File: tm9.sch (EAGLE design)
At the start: 42 parts, among them J1 DF23C-10DP-0.5V(92), J2 DF23C-10DP-0.5V(92), U2 ARTEMIS_MODULESMD, Y1 32.768kHz

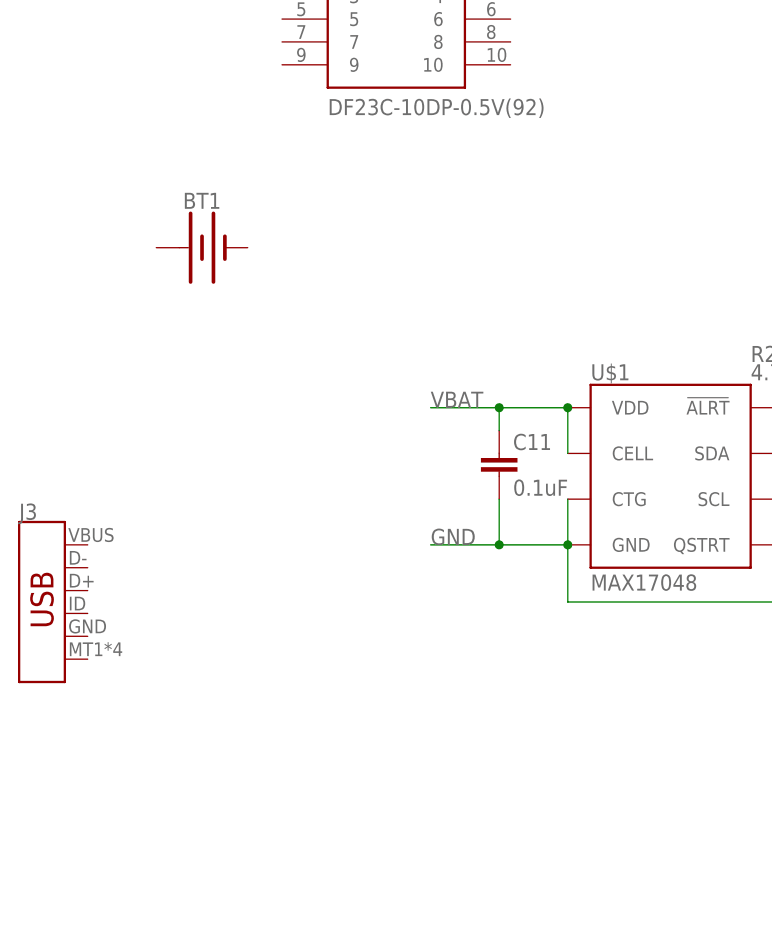
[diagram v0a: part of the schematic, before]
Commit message: rough draft
added JST-SH 6-pin RA connector, 1mA battery, and just shuffled around parts to get a general feel for things. Just a very rough draft.
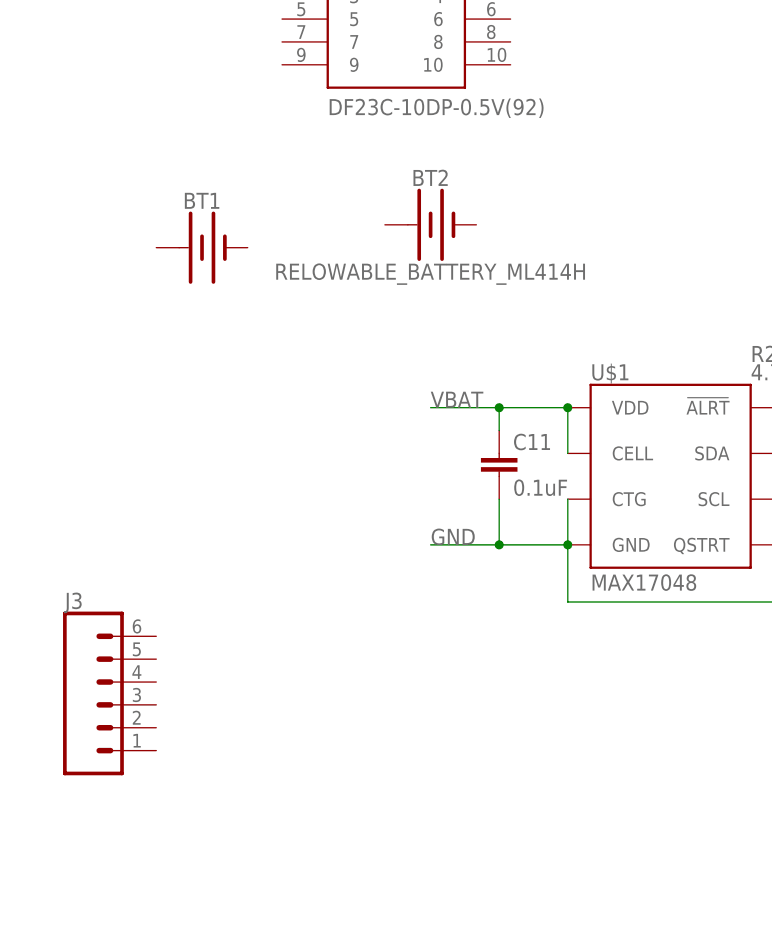
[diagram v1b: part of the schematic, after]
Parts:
- added BT2: RELOWABLE_BATTERY_ML414H, SparkFun-Batteries:RELOWABLE_BATTERY_ML414H
- J3: device SparkFun-Connectors:USB_MICRO-B_SMT -> SparkFun-Connectors:CONN_06JST-SMD-LOCKING
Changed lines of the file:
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@@
 <part name="J2" library="DF23C-10DP-0.5V_92_" deviceset="DF23C-10DP-0.5V(92)" device=""/>
 <part name="U2" library="SparkFun-IC-Microcontroller" deviceset="ARTEMIS_MODULE" device="SMD"/>
-<part name="J3" library="SparkFun-Connectors" deviceset="USB_MICRO-B" device="_SMT"/>
 <part name="BT1" library="SparkFun-Batteries" deviceset="BATTERY" device="-20MM_SMD_4LEGS_OVERPASTE_INNER"/>
+<part name="J3" library="SparkFun-Connectors" deviceset="CONN_06" device="JST-SMD-LOCKING"/>
+<part name="BT2" library="SparkFun-Batteries" deviceset="RELOWABLE_BATTERY" device="_ML414H"/>
 </parts>
 <sheets>
@@
 <attribute name="VALUE" x="68.58" y="7.62" size="1.778" layer="96"/>
 </instance>
-<instance part="J3" gate="J1" x="-121.92" y="101.6" smashed="yes">
-<attribute name="VALUE" x="-124.46" y="91.694" size="1.778" layer="96" font="vector" rot="MR180" align="top-left"/>
-<attribute name="NAME" x="-124.46" y="112.014" size="1.778" layer="95" font="vector"/>
-</instance>
 <instance part="BT1" gate="G$1" x="-104.14" y="142.24" smashed="yes">
 <attribute name="NAME" x="-104.14" y="146.558" size="1.778" layer="95" font="vector" align="bottom-center"/>
 <attribute name="VALUE" x="-104.14" y="137.922" size="1.778" layer="96" font="vector" align="top-center"/>
 </instance>
+<instance part="J3" gate="JP1" x="-114.3" y="91.44" smashed="yes">
+<attribute name="VALUE" x="-119.38" y="81.534" size="1.778" layer="96" font="vector"/>
+<attribute name="NAME" x="-119.38" y="102.108" size="1.778" layer="95" font="vector"/>
+</instance>
+<instance part="BT2" gate="G$1" x="-78.74" y="144.78" smashed="yes">
+<attribute name="NAME" x="-78.74" y="149.098" size="1.778" layer="95" font="vector" align="bottom-center"/>
+<attribute name="VALUE" x="-78.74" y="140.462" size="1.778" layer="96" font="vector" align="top-center"/>
+</instance>
 </instances>

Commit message: added SCL and SDA labels
added SCL and SDA labels for all I2C ports on Artemis module.

labeled both I2C LCDs accordingly for shortest I2C trace length.
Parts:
- added U1: SST25VF020BUSON, SparkFun-IC-Memory:SST25VF020BUSON
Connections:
- new net SCL0: U2.(SCL0/SCK0)~D5
- new net SCL2: LCD1.4, R1.1, U2.(SCL2/SCK2)~D27
- new net SCL3: U2.(SCL3/SCK3/TX1)~D42
- new net SCL4: U2.(SCL4/SCK4/TX1)~D39
- new net SDA0: U2.(SDA0/SDI0/I2SDAT)~D6
- new net SDA2: LCD1.5, R2.1, U2.(SDA2/SDI2/RX1)~D25
- new net SDA3: U2.(SDA3/SDI3/RX1)~D43
- new net SDA4: U2.(SDA4/SDI4/RX1)D40
- net SCL: no longer LCD1.4, R1.1
- net SCL1: now also U2.(SCL1/SCK1/TX1/SCCLK)D8
- net SDA: no longer LCD1.5, R2.1
- net SDA1: now also U2.(SDA1/SDI1/RX1/SCCIO)D9
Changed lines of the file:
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@@
 <setting verticaltext="up"/>
 </settings>
-<grid distance="0.1" unitdist="inch" unit="inch" style="lines" multiple="1" display="no" altdistance="0.01" altunitdist="inch" altunit="inch"/>
+<grid distance="0.1" unitdist="inch" unit="inch" style="lines" multiple="1" display="yes" altdistance="0.01" altunitdist="inch" altunit="inch"/>
 <layers>
 <layer number="1" name="Top" color="4" fill="1" visible="no" active="no"/>
@@
 <part name="J3" library="SparkFun-Connectors" deviceset="CONN_06" device="JST-SMD-LOCKING"/>
 <part name="BT2" library="SparkFun-Batteries" deviceset="RELOWABLE_BATTERY" device="_ML414H"/>
+<part name="U1" library="SparkFun-IC-Memory" deviceset="SST25VF020B" device="USON"/>
 </parts>
 <sheets>
@@
 <attribute name="NAME" x="-78.74" y="149.098" size="1.778" layer="95" font="vector" align="bottom-center"/>
 <attribute name="VALUE" x="-78.74" y="140.462" size="1.778" layer="96" font="vector" align="top-center"/>
+</instance>
+<instance part="U1" gate="G$1" x="114.3" y="162.56" smashed="yes">
+<attribute name="NAME" x="104.14" y="167.894" size="1.778" layer="95" font="vector"/>
+<attribute name="VALUE" x="104.14" y="154.686" size="1.778" layer="96" font="vector" align="top-left"/>
 </instance>
 </instances>
@@
 <net name="SCL" class="0">
 <segment>
-<pinref part="LCD1" gate="G$1" pin="4"/>
-<wire x1="99.06" y1="134.62" x2="99.06" y2="129.54" width="0.1524" layer="91"/>
-<wire x1="99.06" y1="116.84" x2="99.06" y2="129.54" width="0.1524" layer="91"/>
-<label x="99.06" y="116.84" size="1.778" layer="95" rot="R90"/>
-<pinref part="R1" gate="G$1" pin="1"/>
-<wire x1="104.14" y1="129.54" x2="99.06" y2="129.54" width="0.1524" layer="91"/>
-<junction x="99.06" y="129.54"/>
-</segment>
-<segment>
 <wire x1="-40.64" y1="114.3" x2="-38.1" y2="114.3" width="0.1524" layer="91"/>
 <label x="-33.02" y="114.3" size="1.778" layer="95"/>
@@
 </net>
 <net name="SDA" class="0">
-<segment>
-<pinref part="LCD1" gate="G$1" pin="5"/>
-<wire x1="101.6" y1="127" x2="101.6" y2="134.62" width="0.1524" layer="91"/>
-<label x="101.6" y="116.84" size="1.778" layer="95" rot="R90"/>
-<pinref part="R2" gate="G$1" pin="1"/>
-<wire x1="101.6" y1="127" x2="101.6" y2="116.84" width="0.1524" layer="91"/>
-<wire x1="104.14" y1="127" x2="101.6" y2="127" width="0.1524" layer="91"/>
-<junction x="101.6" y="127"/>
-</segment>
 <segment>
 <wire x1="-40.64" y1="119.38" x2="-35.56" y2="119.38" width="0.1524" layer="91"/>
@@
 <junction x="134.62" y="127"/>
 </segment>
+<segment>
+<pinref part="U2" gate="U1" pin="(SDA1/SDI1/RX1/SCCIO)D9"/>
+<wire x1="134.62" y1="71.12" x2="144.78" y2="71.12" width="0.1524" layer="91"/>
+<label x="139.7" y="71.12" size="1.778" layer="95"/>
+</segment>
 </net>
 <net name="SCL1" class="0">
@@
 <junction x="132.08" y="129.54"/>
 </segment>
+<segment>
+<pinref part="U2" gate="U1" pin="(SCL1/SCK1/TX1/SCCLK)D8"/>
+<wire x1="134.62" y1="73.66" x2="144.78" y2="73.66" width="0.1524" layer="91"/>
+<label x="139.7" y="73.66" size="1.778" layer="95"/>
+</segment>
 </net>
 <net name="ALT" class="0">
@@
 </segment>
 </net>
+<net name="SCL0" class="0">
+<segment>
+<pinref part="U2" gate="U1" pin="(SCL0/SCK0)~D5"/>
+<wire x1="134.62" y1="81.28" x2="144.78" y2="81.28" width="0.1524" layer="91"/>
+<label x="139.7" y="81.28" size="1.778" layer="95"/>
+</segment>
+</net>
+<net name="SDA0" class="0">
+<segment>
+<pinref part="U2" gate="U1" pin="(SDA0/SDI0/I2SDAT)~D6"/>
+<wire x1="134.62" y1="78.74" x2="144.78" y2="78.74" width="0.1524" layer="91"/>
+<label x="139.7" y="78.74" size="1.778" layer="95"/>
+</segment>
+</net>
+<net name="SDA2" class="0">
+<segment>
+<pinref part="U2" gate="U1" pin="(SDA2/SDI2/RX1)~D25"/>
+<wire x1="134.62" y1="45.72" x2="144.78" y2="45.72" width="0.1524" layer="91"/>
+<label x="139.7" y="45.72" size="1.778" layer="95"/>
+</segment>
+<segment>
+<pinref part="LCD1" gate="G$1" pin="5"/>
+<wire x1="101.6" y1="127" x2="101.6" y2="134.62" width="0.1524" layer="91"/>
+<label x="101.6" y="116.84" size="1.778" layer="95" rot="R90"/>
+<pinref part="R2" gate="G$1" pin="1"/>
+<wire x1="101.6" y1="127" x2="101.6" y2="116.84" width="0.1524" layer="91"/>
+<wire x1="104.14" y1="127" x2="101.6" y2="127" width="0.1524" layer="91"/>
+<junction x="101.6" y="127"/>
+</segment>
+</net>
+<net name="SCL2" class="0">
+<segment>
+<pinref part="U2" gate="U1" pin="(SCL2/SCK2)~D27"/>
+<wire x1="134.62" y1="40.64" x2="144.78" y2="40.64" width="0.1524" layer="91"/>
+<label x="139.7" y="40.64" size="1.778" layer="95"/>
+</segment>
+<segment>
+<pinref part="LCD1" gate="G$1" pin="4"/>
+<wire x1="99.06" y1="134.62" x2="99.06" y2="129.54" width="0.1524" layer="91"/>
+<wire x1="99.06" y1="116.84" x2="99.06" y2="129.54" width="0.1524" layer="91"/>
+<label x="99.06" y="116.84" size="1.778" layer="95" rot="R90"/>
+<pinref part="R1" gate="G$1" pin="1"/>
+<wire x1="104.14" y1="129.54" x2="99.06" y2="129.54" width="0.1524" layer="91"/>
+<junction x="99.06" y="129.54"/>
+</segment>
+</net>
+<net name="SCL4" class="0">
+<segment>
+<pinref part="U2" gate="U1" pin="(SCL4/SCK4/TX1)~D39"/>
+<wire x1="134.62" y1="27.94" x2="144.78" y2="27.94" width="0.1524" layer="91"/>
+<label x="139.7" y="27.94" size="1.778" layer="95"/>
+</segment>
+</net>
+<net name="SDA4" class="0">
+<segment>
+<pinref part="U2" gate="U1" pin="(SDA4/SDI4/RX1)D40"/>
+<wire x1="144.78" y1="25.4" x2="134.62" y2="25.4" width="0.1524" layer="91"/>
+<label x="139.7" y="25.4" size="1.778" layer="95"/>
+</segment>
+</net>
+<net name="SCL3" class="0">
+<segment>
+<pinref part="U2" gate="U1" pin="(SCL3/SCK3/TX1)~D42"/>
+<wire x1="134.62" y1="20.32" x2="144.78" y2="20.32" width="0.1524" layer="91"/>
+<label x="139.7" y="20.32" size="1.778" layer="95"/>
+</segment>
+</net>
+<net name="SDA3" class="0">
+<segment>
+<pinref part="U2" gate="U1" pin="(SDA3/SDI3/RX1)~D43"/>
+<wire x1="144.78" y1="17.78" x2="134.62" y2="17.78" width="0.1524" layer="91"/>
+<label x="139.7" y="17.78" size="1.778" layer="95"/>
+</segment>
+</net>
